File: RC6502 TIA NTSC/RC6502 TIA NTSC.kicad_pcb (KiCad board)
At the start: 2 copper layers, 99.1 x 99.7 mm, 34 parts, among them J1 RC6502_Backplane, J2 VDU_BASE, J3 VIDEO, J4 Hole, J5 Hole, J6 Hole, J7 Hole, J8 RCA_PLUG, U1 MC6847, U10 74LS02, U11 VDU_Port, U12 74LS374, U2 HM62256BLP-7, U3 74LS244, U4 74LS244, U5 74LS245, U6 74LS374, U7 74HCT138, U8 74LS32, U9 74HCT138, X1 3.579545 MHz

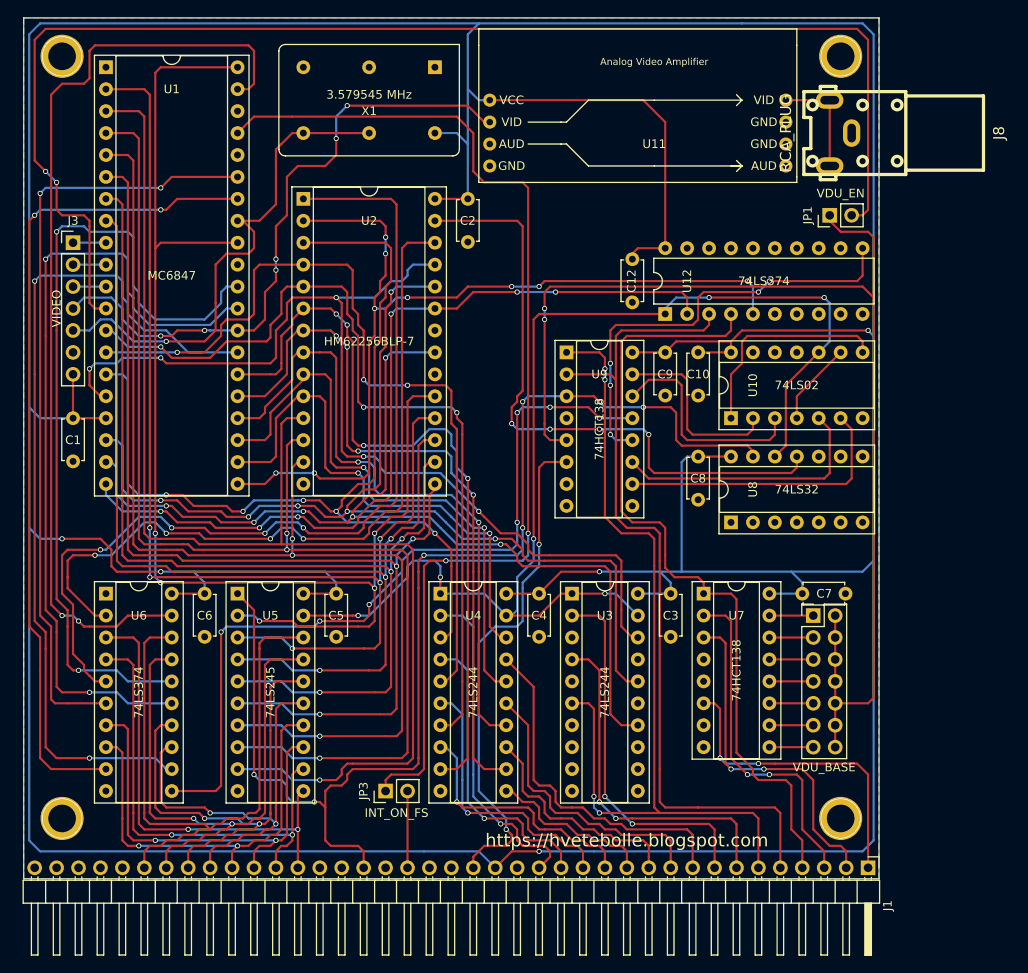
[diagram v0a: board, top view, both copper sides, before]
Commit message: TIA layout done
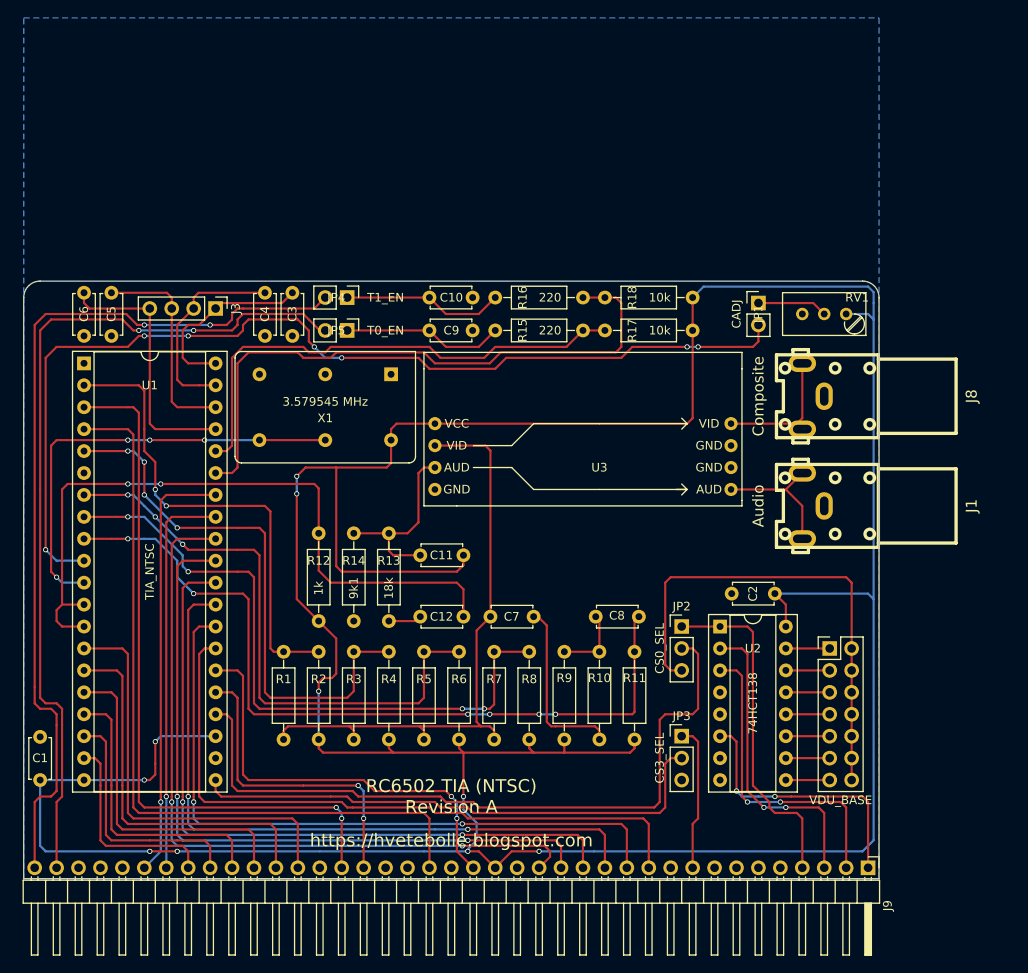
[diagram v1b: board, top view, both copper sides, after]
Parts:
- removed J4, J5, J6, J7: Hole, mounting:Mounting
- removed U10: 74LS02, Housings_DIP:DIP-14_W7.62mm_Socket
- removed U12: 74LS374, Housings_DIP:DIP-20_W7.62mm
- removed the U2 at (85.1, 65.4)
- removed the U3 at (116.2, 111.1)
- removed U4: 74LS244, Housings_DIP:DIP-20_W7.62mm_Socket
- removed U5: 74LS245, Housings_DIP:DIP-20_W7.62mm_Socket
- removed U6: 74LS374, Housings_DIP:DIP-20_W7.62mm_Socket
- removed U8: 74LS32, Housings_DIP:DIP-14_W7.62mm_Socket
- removed U9: 74HCT138, Housings_DIP:DIP-16_W7.62mm_Socket
- added C11: 820pF, Capacitors_THT:C_Disc_D4.7mm_W2.5mm_P5.00mm, F.Cu at (103.6, 106.7)
- added J9: RC6502_Backplane_Extra, Pin_Headers:Pin_Header_Angled_1x39_Pitch2.54mm, F.Cu at (150.5, 142.9)
- added JP2: CS0_SEL, Pin_Headers:Pin_Header_Straight_1x03_Pitch2.54mm, F.Cu at (128.9, 114.9)
- added JP4: T1_EN, Pin_Headers:Pin_Header_Straight_1x02_Pitch2.54mm, F.Cu at (90.2, 76.8)
- added JP5: T0_EN, Pin_Headers:Pin_Header_Straight_1x02_Pitch2.54mm, F.Cu at (90.2, 80.6)
- added R1: 27k, Resistors_THT:R_Axial_DIN0207_L6.3mm_D2.5mm_P10.16mm_Horizontal, F.Cu at (82.8, 117.9)
- added R10: 6k8, Resistors_THT:R_Axial_DIN0207_L6.3mm_D2.5mm_P10.16mm_Horizontal, F.Cu at (119.4, 117.9)
- added R11: 1k, Resistors_THT:R_Axial_DIN0207_L6.3mm_D2.5mm_P10.16mm_Horizontal, F.Cu at (123.4, 117.9)
- added R12: 1k, Resistors_THT:R_Axial_DIN0207_L6.3mm_D2.5mm_P10.16mm_Horizontal, F.Cu at (86.9, 104.1)
- added R13: 18k, Resistors_THT:R_Axial_DIN0207_L6.3mm_D2.5mm_P10.16mm_Horizontal, F.Cu at (95.0, 104.1)
- added R14: 9k1, Resistors_THT:R_Axial_DIN0207_L6.3mm_D2.5mm_P10.16mm_Horizontal, F.Cu at (90.9, 104.1)
- added R15: 220, Resistors_THT:R_Axial_DIN0207_L6.3mm_D2.5mm_P10.16mm_Horizontal, F.Cu at (117.5, 80.6)
- added R16: 220, Resistors_THT:R_Axial_DIN0207_L6.3mm_D2.5mm_P10.16mm_Horizontal, F.Cu at (117.5, 76.8)
- added R17: 10k, Resistors_THT:R_Axial_DIN0207_L6.3mm_D2.5mm_P10.16mm_Horizontal, F.Cu at (130.2, 80.6)
- added R18: 10k, Resistors_THT:R_Axial_DIN0207_L6.3mm_D2.5mm_P10.16mm_Horizontal, F.Cu at (130.2, 76.8)
- added R2: 3K3, Resistors_THT:R_Axial_DIN0207_L6.3mm_D2.5mm_P10.16mm_Horizontal, F.Cu at (86.9, 117.9)
- added R3: 56k, Resistors_THT:R_Axial_DIN0207_L6.3mm_D2.5mm_P10.16mm_Horizontal, F.Cu at (90.9, 117.9)
- added R4: 3K3, Resistors_THT:R_Axial_DIN0207_L6.3mm_D2.5mm_P10.16mm_Horizontal, F.Cu at (95.0, 117.9)
- added R5: 27K, Resistors_THT:R_Axial_DIN0207_L6.3mm_D2.5mm_P10.16mm_Horizontal, F.Cu at (99.1, 117.9)
- added R6: 3K3, Resistors_THT:R_Axial_DIN0207_L6.3mm_D2.5mm_P10.16mm_Horizontal, F.Cu at (103.1, 117.9)
- added R7: 110k, Resistors_THT:R_Axial_DIN0207_L6.3mm_D2.5mm_P10.16mm_Horizontal, F.Cu at (107.2, 117.9)
- added R8: 3K3, Resistors_THT:R_Axial_DIN0207_L6.3mm_D2.5mm_P10.16mm_Horizontal, F.Cu at (111.3, 117.9)
- added R9: 1k, Resistors_THT:R_Axial_DIN0207_L6.3mm_D2.5mm_P10.16mm_Horizontal, F.Cu at (115.3, 117.9)
- added RV1: 500k, Potentiometers:Potentiometer_Trimmer_Bourns_3296W, F.Cu at (148.0, 78.7)
- C10, C9: value 100nF -> 470pF
- C3, C4, C5, C6: value 100nF -> 68nF
- C7: value 100nF -> 22pF
- C8: value 100nF -> 47pF
- J1: value RC6502_Backplane -> Audio; footprint Pin_Headers:Pin_Header_Angled_1x39_Pitch2.54mm -> RCA:rca_yellow
- J3: value VIDEO -> P; footprint Pin_Headers:Pin_Header_Straight_1x07_Pitch2.54mm -> Pin_Headers:Pin_Header_Straight_1x04_Pitch2.54mm
- J8: value RCA_PLUG -> Composite; footprint rca:rca_yellow -> RCA:rca_yellow
- JP1: value VDU_EN -> CADJ
- JP3: value INT_ON_FS -> CS3_SEL; footprint Pin_Headers:Pin_Header_Straight_1x02_Pitch2.54mm -> Pin_Headers:Pin_Header_Straight_1x03_Pitch2.54mm
- U1: value MC6847 -> TIA_NTSC
- moved C2 57.9 mm to (139.7, 111.1), turned to 180 degrees
- moved C3 53.0 mm to (83.8, 81.3), turned to 90 degrees
- moved C12 45.8 mm to (103.6, 113.8), turned to 180 degrees
- moved C4 43.6 mm to (80.6, 81.3), turned to 90 degrees
- moved C1 42.1 mm to (54.6, 132.7), turned to 90 degrees
- moved J1 42.1 mm to (146.7, 101.0), turned to 90 degrees
- moved C5 39.6 mm to (62.9, 81.3), turned to 90 degrees
- moved U3 38.0 mm to (119.4, 95.2)
- moved X1 35.9 mm to (95.2, 85.7)
- moved JP3 34.9 mm to (128.9, 127.6), turned to 0 degrees
- moved U1 34.4 mm to (59.7, 84.5)
- moved C6 33.0 mm to (59.7, 81.3), turned to 90 degrees
- moved C10 31.8 mm to (99.7, 76.8), turned to 0 degrees
- moved C7 31.2 mm to (111.8, 113.8), turned to 180 degrees
- moved J8 30.6 mm to (146.7, 88.3)
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- renumbered U7 to U2, U11 to U3
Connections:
- C10 pad 1: VCC -> /T1_IN
- C12 pad 1: VCC -> /AUD0
- C12 pad 2: GND -> Net-(C12-Pad2)
- C3 pad 1: VCC -> GND
- C3 pad 2: GND -> /P0
- C4 pad 1: VCC -> GND
- C4 pad 2: GND -> /P1
- C5 pad 1: VCC -> GND
- C5 pad 2: GND -> /P2
- C6 pad 1: VCC -> GND
- C6 pad 2: GND -> /P3
- C7 pad 1: VCC -> Net-(C7-Pad1)
- C7 pad 2: GND -> VIDEO
- C8 pad 1: VCC -> /COLOR
- C8 pad 2: GND -> Net-(C8-Pad2)
- C9 pad 1: VCC -> /T0_IN
- J1 pad 1: A15 -> GND
- J1 pad 2: A14 -> Net-(J1-Pad2)
- J2 pad 10: VDU_BASE -> TIA_BASE
- J2 pad 12: VDU_BASE -> TIA_BASE
- J2 pad 14: VDU_BASE -> TIA_BASE
- J2 pad 2: VDU_BASE -> TIA_BASE
- J2 pad 4: VDU_BASE -> TIA_BASE
- J2 pad 6: VDU_BASE -> TIA_BASE
- J2 pad 8: VDU_BASE -> TIA_BASE
- J3 pad 1: Net-(J3-Pad1) -> /P0
- J3 pad 2: Net-(J3-Pad2) -> /P1
- J3 pad 3: Net-(J3-Pad3) -> /P2
- J3 pad 4: Y -> /P3
- JP1 pad 1: VDU_BASE -> Net-(JP1-Pad1)
- JP1 pad 2: ~VDU_DISABLE -> /CADJ
- JP3 pad 1: ~FS -> /A7
- JP3 pad 2: Net-(J1-Pad22) -> /~CS3
- U1 pad 10: Net-(J3-Pad2) -> /CADJ
- U1 pad 11: Net-(J3-Pad3) -> /OSC_IN
- U1 pad 12: ~VDU_DISABLE -> /AUD0
- U1 pad 13: VA5 -> /AUD0
- U1 pad 14: VA6 -> /D0
- U1 pad 15: VA7 -> /D1
- U1 pad 16: VA8 -> /D2
- U1 pad 17: VCC -> /D3
- U1 pad 18: VA9 -> /D4
- U1 pad 19: VA10 -> /D5
- U1 pad 2: VD6 -> /CSYNC
- U1 pad 20: VA11 -> VCC
- U1 pad 21: VA12 -> /~CS3
- U1 pad 22: VA0 -> GND
- U1 pad 23: VA1 -> VCC
- U1 pad 24: VA2 -> /~CS0
- U1 pad 25: VA3 -> /R/~W
- U1 pad 26: VA4 -> /PHI2
- U1 pad 27: GM2 -> /A5
- U1 pad 28: Y -> /A4
- U1 pad 29: GM1 -> /A3
- U1 pad 3: VD0 -> /RDY
- U1 pad 30: GM0 -> /A2
- U1 pad 31: GND -> /A1
- U1 pad 32: VD7 -> /A0
- U1 pad 33: VDU_CLK -> /D6
- U1 pad 34: S/~A -> /D7
- U1 pad 35: G/~A -> /T1
- U1 pad 36: (no net) -> /T0
- U1 pad 37: ~FS -> /P3
- U1 pad 38: (no net) -> /P2
- U1 pad 39: CSS -> /P1
- U1 pad 4: VD1 -> /PHI0
- U1 pad 40: VD7 -> /P0
- U1 pad 5: VD2 -> /LUM1
- U1 pad 6: VD3 -> (no net)
- U1 pad 7: VD4 -> /LUM2
- U1 pad 8: VD5 -> /LUM0
- U1 pad 9: Net-(J3-Pad1) -> /COLOR
- U2 pad 1: A12 -> /A12
- U2 pad 2: A13 -> /A13
- U2 pad 3: A14 -> /A14
- U2 pad 6: A15 -> /A15
- U3 pad 2: Y -> VIDEO
- U3 pad 4: (no net) -> AUDIO
- U3 pad 5: (no net) -> Net-(J1-Pad2)
- X1 pad 8: VDU_CLK -> /OSC_IN
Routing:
- net VCC: track 635.3 -> 421.4 mm, vias 5 -> 10
- net ~VDU_DISABLE: track 156.8 -> 0.00 mm, vias 2 -> 0
- net VD7: track 151.7 -> 0.00 mm, vias 5 -> 0
- net VD0: track 148.0 -> 0.00 mm, vias 1 -> 0
- net R/~W: track 142.7 -> 0.00 mm, vias 7 -> 0
- net ~CS_RAM_EXT: track 141.7 -> 0.00 mm, vias 6 -> 0
- net VD1: track 139.9 -> 0.00 mm, vias 3 -> 0
- net VDU_BASE: track 138.0 -> 0.00 mm, vias 2 -> 0
- net VD6: track 136.0 -> 0.00 mm, vias 5 -> 0
- net VD2: track 131.0 -> 0.00 mm, vias 3 -> 0
- net ~FS: track 125.3 -> 0.00 mm, vias 2 -> 0
- net VD3: track 125.1 -> 0.00 mm, vias 3 -> 0
- net VD4: track 122.5 -> 0.00 mm, vias 3 -> 0
- net VD5: track 120.0 -> 0.00 mm, vias 3 -> 0
- net VA8: track 119.7 -> 0.00 mm, vias 5 -> 0
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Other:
- board size 99.1 x 99.7 mm -> 99.1 x 69.2 mm
- board text added: "RC6502 TIA (NTSC) Revision A"
- board text removed: "Address Buffer #0 A00-A07"
- board text removed: "Address Buffer #1 A08-A10"
- board text removed: "Analog Video Amplifier"
- board text removed: "Analog Video Amplifier Attach adjusted analog composite video circuit suitable for display used, added as option to test assorted design viability."
- board text removed: "Data Transceiver"
- board text removed: "MC6847 Video Display Generator"
- board text removed: "RC6502 VDU Board Revision A https://hvetebolle.blogspot.com"
- board text removed: "Register 0: [b0,1] Page select [b2] G/~A [b03] S/~A [b04] GM2 [b05] GM1 [b06] GM0 [b07] CSS"
- board text removed: "Register 1: [b0,1] Video RAM Window Select (external access)"
- board text removed: "VDU Clock NTSC freq. oscillator"
- board text removed: "VDU Register 0 (Page Select/Settings) VDU_BASE + $800"
- board text removed: "VDU Register 1 (Memory Window Select) VDU_BASE + $C00"
- board text removed: "Video RAM VDU_BASE + [$000-$7FF] Register 0[b0-b1] 8K Page Select Register 1[b0-b1] 2K Window Select"

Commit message: Moved CADJ potentiometer
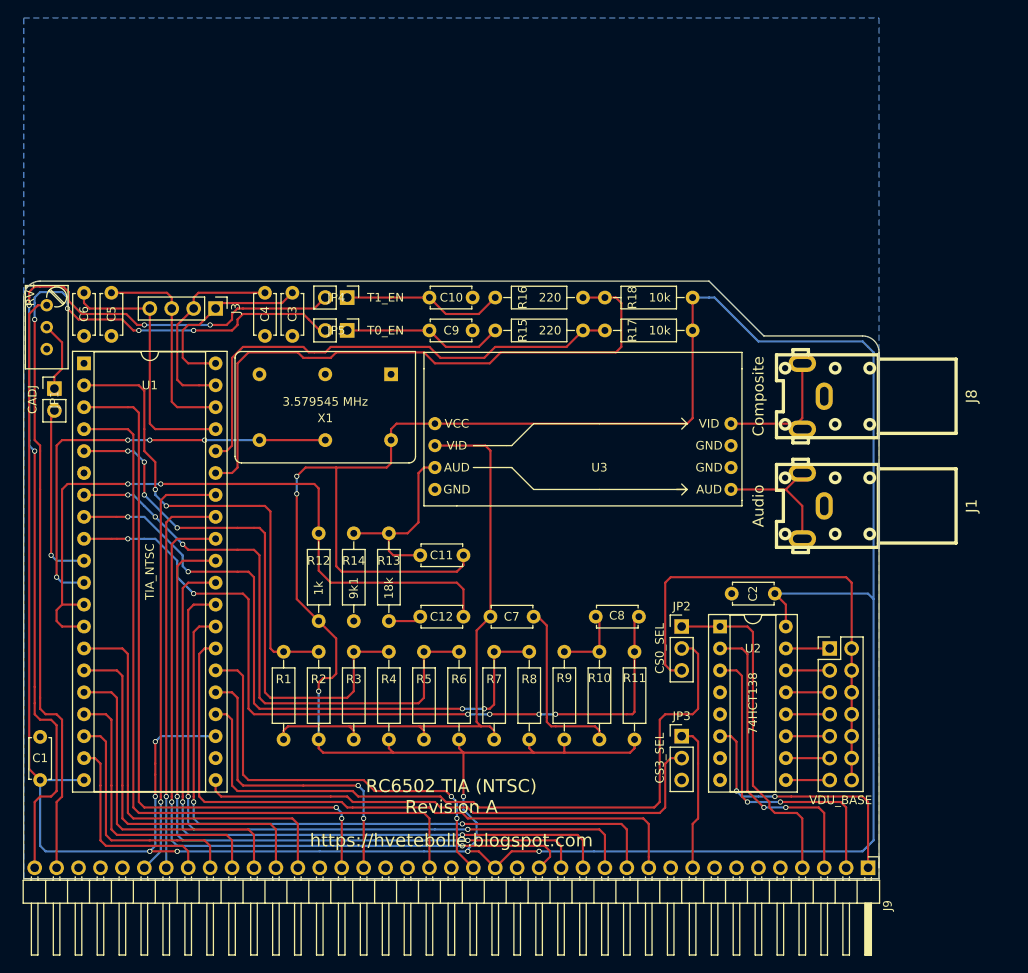
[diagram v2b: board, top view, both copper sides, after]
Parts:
- moved RV1 92.6 mm to (55.4, 77.7), turned to 90 degrees
- moved JP1 82.1 mm to (56.3, 87.4)
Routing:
- net /CADJ: track 118.3 -> 21.0 mm, vias 7 -> 1
- net VCC: track 421.4 -> 470.4 mm
- net Net-(J9-Pad39): track 102.9 -> 109.5 mm, vias 2 -> 4
- net Net-(J9-Pad38): track 100.3 -> 106.8 mm, vias 2 -> 4
- net /OSC_IN: track 51.0 -> 50.1 mm
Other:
- outline, holes or cut-outs redrawn

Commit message: Silkscreen details added
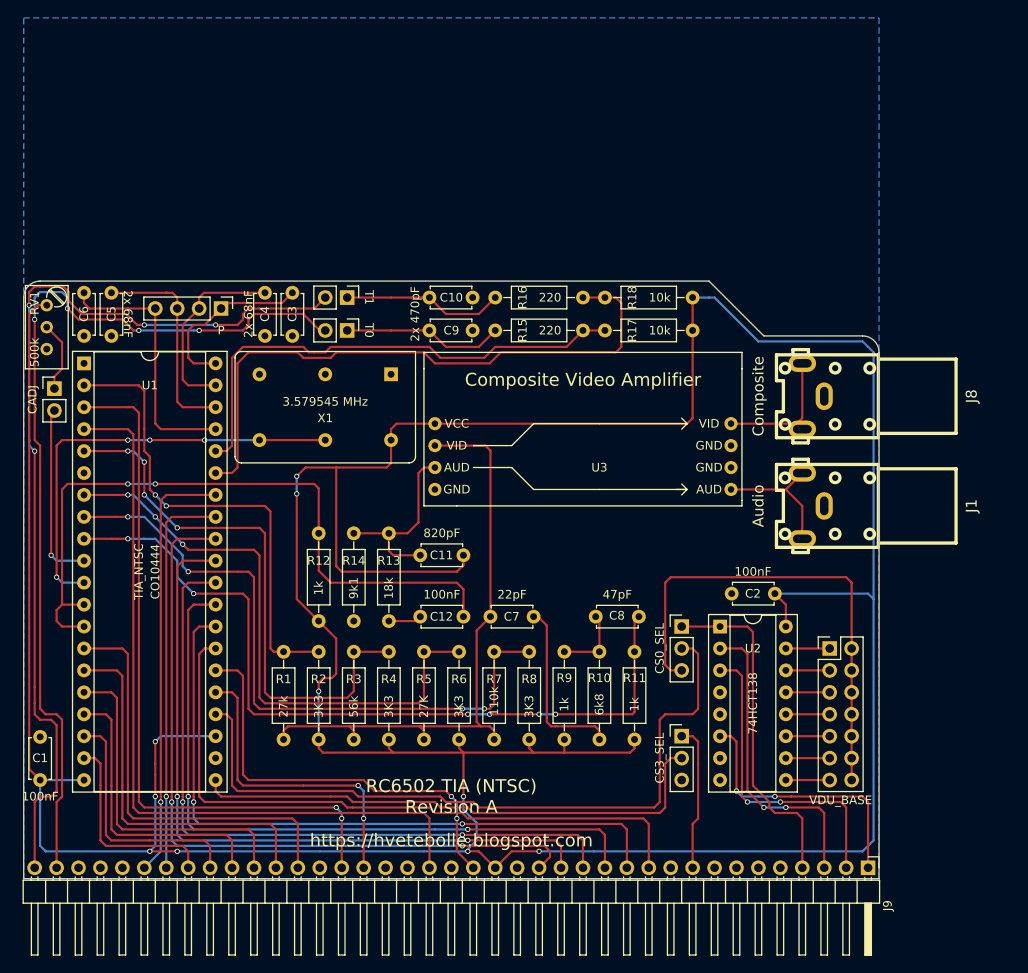
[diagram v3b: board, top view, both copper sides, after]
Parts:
- moved J3 0.63 mm to (75.6, 78.1)
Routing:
- net /P1: track 23.5 -> 22.2 mm
- net /P0: track 21.8 -> 20.5 mm
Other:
- board text added: "1-2 Atari 2600 2-3 RC6502"
- board text added: "2x 470pF"
- board text added: "2x 68nF"
- board text added: "3.579545 MHz"
- board text added: "ANALOG INPUT"
- board text added: "AUDIO"
- board text added: "BUS EN"
- board text added: "CO10444"
- board text added: "COLOR DELAY ADJUST"
- board text added: "Composite Video Amplifier"
- board text added: "NTSC Oscillator"
- board text added: "PIN 1"
- board text added: "T0"
- board text added: "T1"
- board text added: "Television Interface Adapter (TIA) CO10444"
- board text added: "VIDEO"
- board text added: "~CS0"
- board text added: "~CS3"

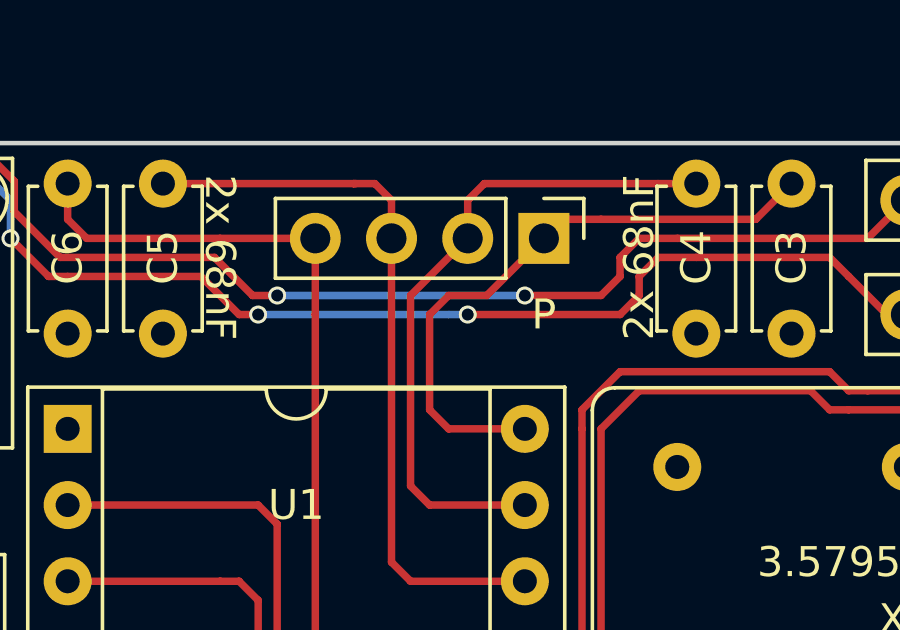
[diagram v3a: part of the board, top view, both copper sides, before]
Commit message: Renamed P to analog to match RIOT
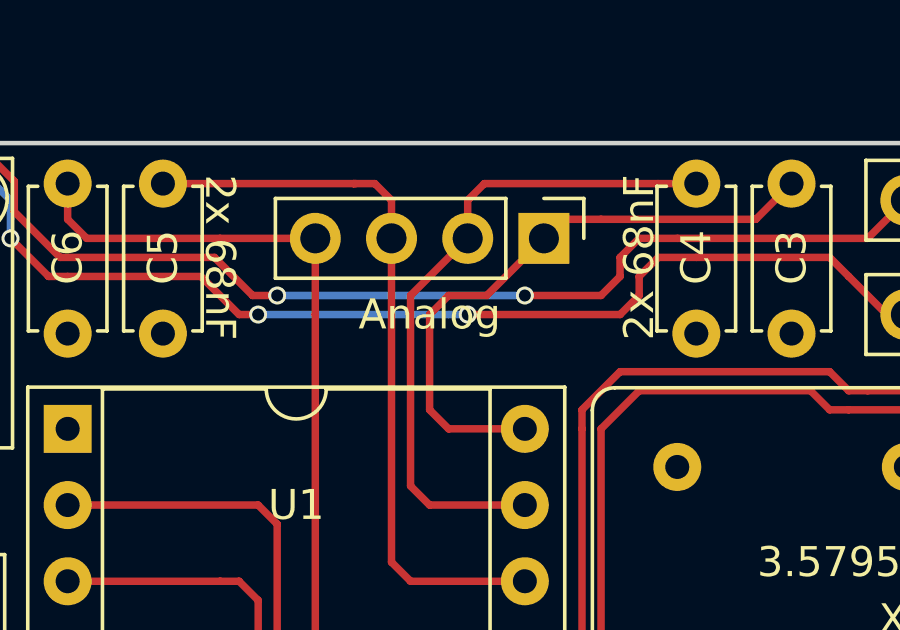
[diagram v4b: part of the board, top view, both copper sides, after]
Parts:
- J3: value P -> Analog
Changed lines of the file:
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@@
       (effects (font (size 1 1) (thickness 0.15)))
     )
-    (fp_text value P (at 2.54 0 360) (layer F.SilkS)
+    (fp_text value Analog (at 2.54 3.81 360) (layer F.SilkS)
       (effects (font (size 1 1) (thickness 0.15)))
     )
